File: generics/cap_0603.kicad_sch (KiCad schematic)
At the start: 4 parts

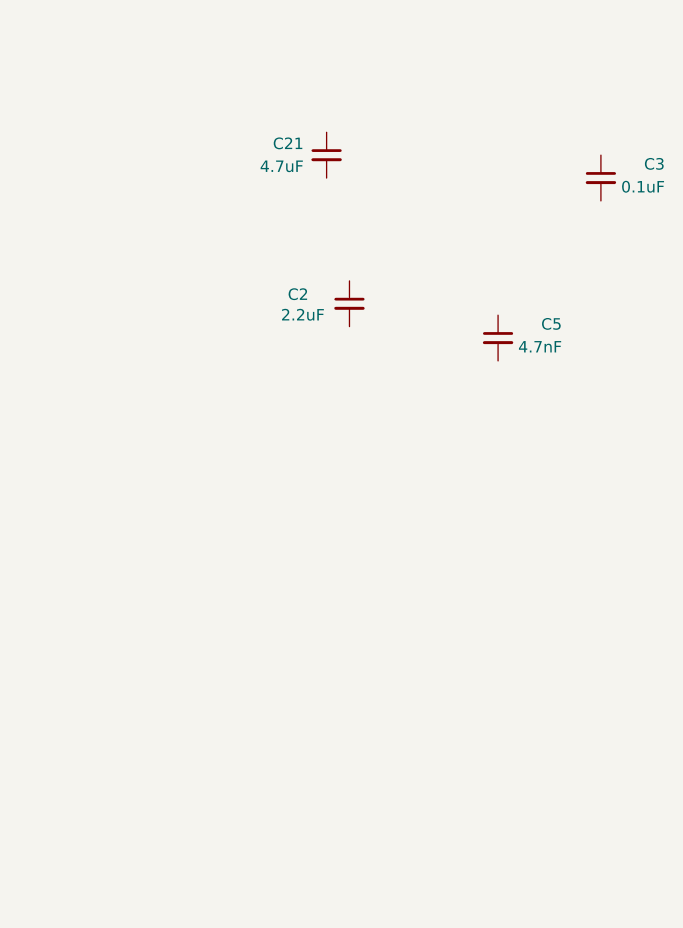
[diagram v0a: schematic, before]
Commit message: Add ESP32 and relevant peripherals
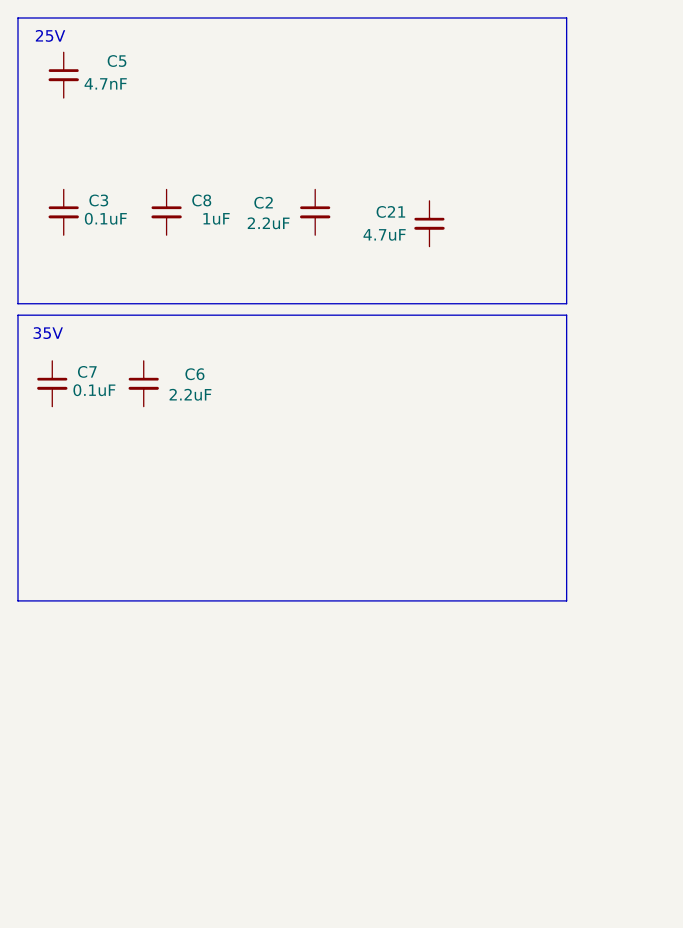
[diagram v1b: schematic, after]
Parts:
- added C6: 2.2uF, Capacitor_SMD:C_0603_1608Metric, symbol Device:C_Small
- added C7: 0.1uF, Resistor_SMD:R_0603_1608Metric, symbol Device:C_Small
- added C8: 1uF, Resistor_SMD:R_0603_1608Metric, symbol Device:C_Small
- C2: footprint Capacitor_SMD:C_0201_0603Metric -> Capacitor_SMD:C_0603_1608Metric; Max Temp (none) -> 85; Tolerance (none) -> 10%; Voltage (none) -> 25V
- C3: Max Temp (none) -> 125
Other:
- note added: "25V"
- note added: "35V"
- moved on the sheet: C2, C21, C3, C5

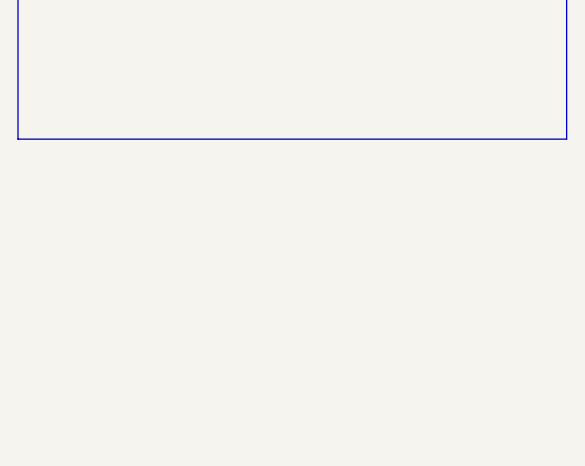
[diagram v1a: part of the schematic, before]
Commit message: Add parts for starter motor
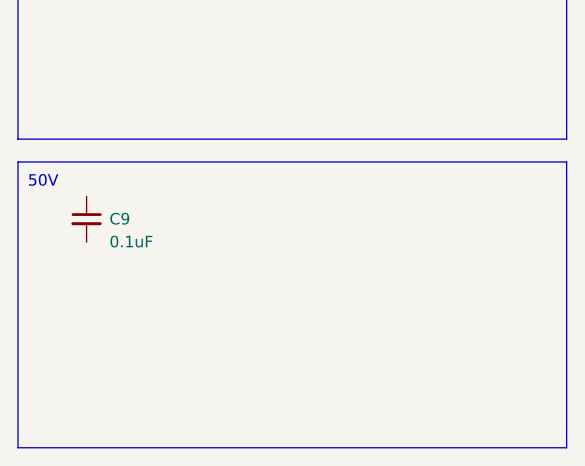
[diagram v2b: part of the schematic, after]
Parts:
- added C9: 0.1uF, Capacitor_SMD:C_0603_1608Metric, symbol Device:C_Small
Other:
- note added: "50V"
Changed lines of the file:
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@@
 	(paper "A4")
+	(rectangle
+		(start 30.48 124.46)
+		(end 91.44 156.21)
+		(stroke
+			(width 0)
+			(type default)
+		)
+		(fill
+			(type none)
+		)
+	)
 	(rectangle
 		(start 30.48 57.15)
@@
 		)
 	)
+	(text "50V"
+		(exclude_from_sim no)
+		(at 33.274 126.746 0)
+		(effects
+			(font
+				(size 1.27 1.27)
+			)
+		)
+	)
 	(symbol
 		(lib_id "Device:C_Small")
@@
 					(unit 1)
 				)
+			)
+		)
+	)
+	(symbol
+		(lib_id "Device:C_Small")
+		(at 38.1 130.81 0)
+		(mirror y)
+		(unit 1)
+		(exclude_from_sim no)
+		(in_bom yes)
+		(on_board yes)
+		(dnp no)
+		(property "Reference" "C9"
+			(at 40.64 130.81 0)
+			(effects
+				(font
+					(size 1.27 1.27)
+				)
+				(justify right)
+			)
+		)
+		(property "Value" "0.1uF"
+			(at 40.64 133.35 0)
+			(effects
+				(font
+					(size 1.27 1.27)
+				)
+				(justify right)
+			)
+		)
+		(property "Footprint" "Capacitor_SMD:C_0603_1608Metric"
+			(at 38.1 130.81 0)
+			(effects
+				(font
+					(size 1.27 1.27)
+				)
+				(hide yes)
+			)
+		)
+		(property "Datasheet" "~"
+			(at 38.1 130.81 0)
+			(effects
+				(font
+					(size 1.27 1.27)
+				)
+				(hide yes)
+			)
+		)
+		(property "Description" "Unpolarized capacitor, small symbol"
+			(at 38.1 130.81 0)
+			(effects
+				(font
+					(size 1.27 1.27)
+				)
+				(hide yes)
+			)
+		)
+		(property "MPN" "CL10B104KB8NNNC "
+			(at 38.1 130.81 0)
+			(effects
+				(font
+					(size 1.27 1.27)
+				)
+				(hide yes)
+			)
+		)
+		(property "Mfr" "Samsung"
+			(at 38.1 130.81 0)
+			(effects
+				(font
+					(size 1.27 1.27)
+				)
+				(hide yes)
+			)
+		)
+		(property "JLCPCB_PN" "C1591"
+			(at 38.1 130.81 0)
+			(effects
+				(font
+					(size 1.27 1.27)
+				)
+				(hide yes)
+			)
+		)
+		(property "Package" "0603"
+			(at 38.1 130.81 0)
+			(effects
+				(font
+					(size 1.27 1.27)
+				)
+				(hide yes)
+			)
+		)
+		(property "Voltage" "50V"
+			(at 38.1 130.81 0)
+			(effects
+				(font
+					(size 1.27 1.27)
+				)
+				(hide yes)
+			)
+		)
+		(property "Tolerance" "10%"
+			(at 38.1 130.81 0)
+			(effects
+				(font
+					(size 1.27 1.27)
+				)
+				(hide yes)
+			)
+		)
+		(property "Dielectric_Class" "X7R"
+			(at 38.1 130.81 0)
+			(effects
+				(font
+					(size 1.27 1.27)
+				)
+				(hide yes)
+			)
+		)
+		(pin "2"
+		)
+		(pin "1"
+		)
+		(instances
+			(project "generics"
+				(path "/ff075d90-2677-48ca-91fd-a3a441ca4e63/78b474d1-d813-4531-98d3-0df205398ee6"
+					(reference "C9")
+					(unit 1)
+				)
